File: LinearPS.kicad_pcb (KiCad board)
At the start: 2 copper layers, 100 x 100 mm, 91 parts, among them J1 Conn_01x03, J2 Conn_01x02, J3 Conn_01x03, J4 Conn_01x01, J5 Conn_01x01, J6 Conn_01x01, J7 Conn_01x01, J8 Conn_01x02, Q1 2N3904, Q2 TIP41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

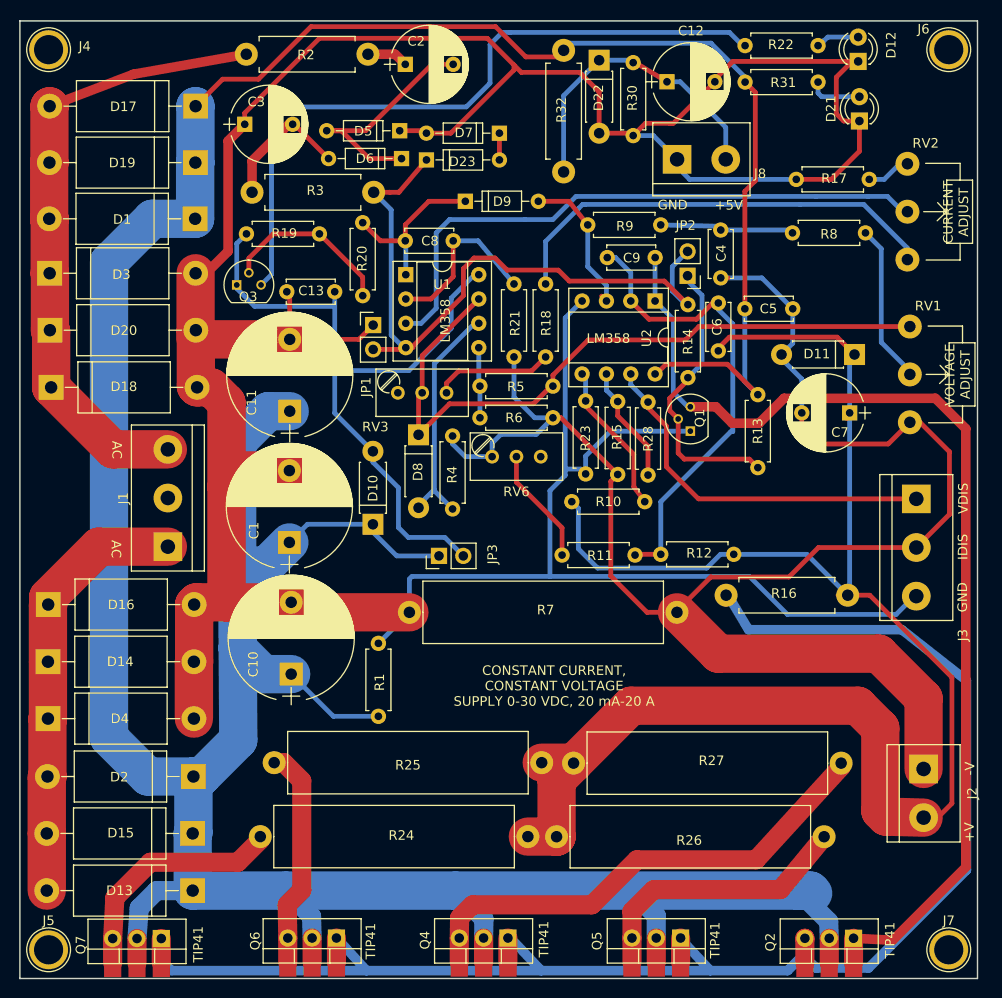
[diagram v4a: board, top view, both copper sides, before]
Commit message: Added external control input for current and voltage
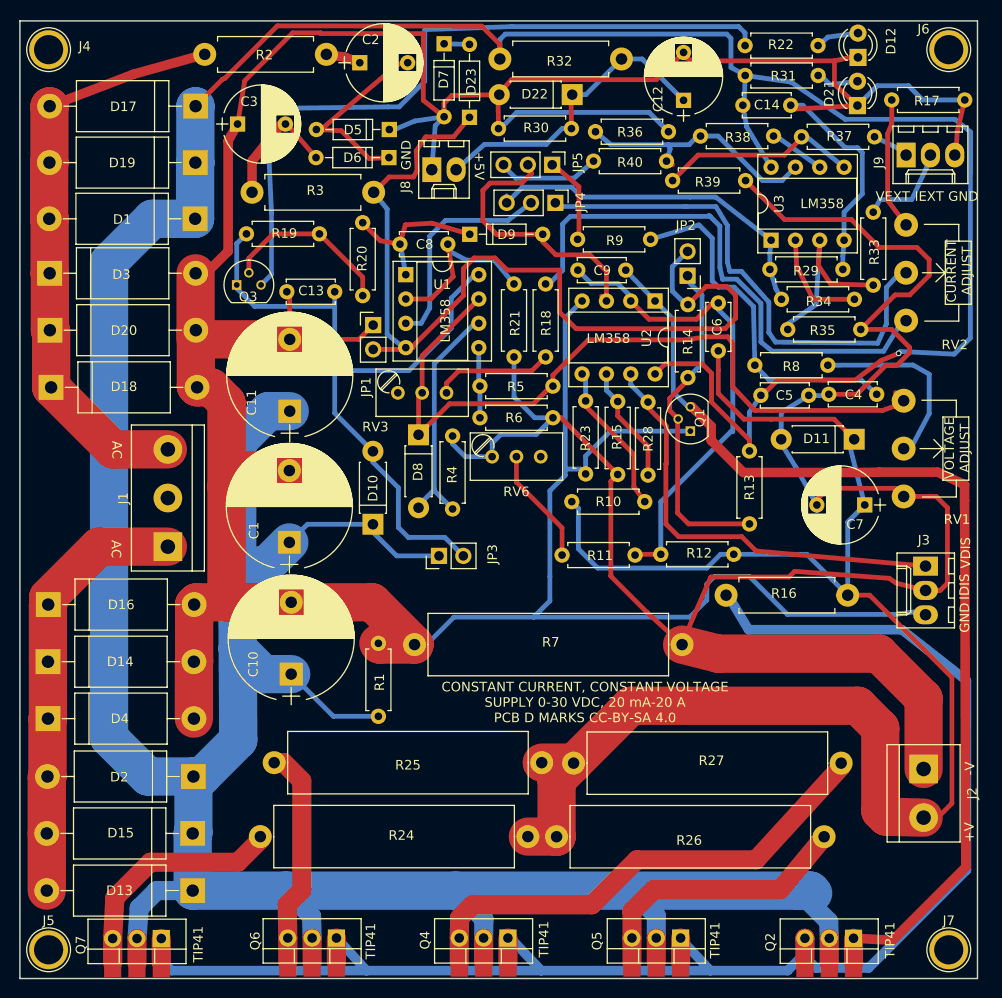
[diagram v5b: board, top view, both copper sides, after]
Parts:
- added C14: 100 nF, Capacitors_THT:C_Disc_D5.0mm_W2.5mm_P5.00mm, F.Cu at (130.5, 58.8)
- added J9: Conn_01x03, Connectors_Molex:Molex_KK-6410-03_03x2.54mm_Straight, F.Cu at (142.5, 64.0)
- added JP4: Jumper_NC_Dual, Pin_Headers:Pin_Header_Straight_1x03_Pitch2.54mm, F.Cu at (105.9, 69.0)
- added JP5: Jumper_NC_Dual, Pin_Headers:Pin_Header_Straight_1x03_Pitch2.54mm, F.Cu at (105.6, 65.0)
- added R29: 10k, Resistors_THT:R_Axial_DIN0207_L6.3mm_D2.5mm_P7.62mm_Horizontal, F.Cu at (128.3, 75.9)
- added R33: 10k, Resistors_THT:R_Axial_DIN0207_L6.3mm_D2.5mm_P7.62mm_Horizontal, F.Cu at (139.1, 77.6)
- added R34: 10k, Resistors_THT:R_Axial_DIN0207_L6.3mm_D2.5mm_P7.62mm_Horizontal, F.Cu at (129.5, 79.1)
- added R35: 10k, Resistors_THT:R_Axial_DIN0207_L6.3mm_D2.5mm_P7.62mm_Horizontal, F.Cu at (130.2, 82.2)
- added R36: 10k, Resistors_THT:R_Axial_DIN0207_L6.3mm_D2.5mm_P7.62mm_Horizontal, F.Cu at (117.7, 61.6)
- added R37: 10k, Resistors_THT:R_Axial_DIN0207_L6.3mm_D2.5mm_P7.62mm_Horizontal, F.Cu at (131.6, 62.1)
- added R38: 10k, Resistors_THT:R_Axial_DIN0207_L6.3mm_D2.5mm_P7.62mm_Horizontal, F.Cu at (128.7, 62.0)
- added R39: 10k, Resistors_THT:R_Axial_DIN0207_L6.3mm_D2.5mm_P7.62mm_Horizontal, F.Cu at (118.2, 66.7)
- added R40: 47k, Resistors_THT:R_Axial_DIN0207_L6.3mm_D2.5mm_P7.62mm_Horizontal, F.Cu at (109.9, 64.6)
- added U3: LM358, Housings_DIP:DIP-8_W7.62mm_Socket, F.Cu at (128.4, 72.9)
- J3: footprint Connectors_Terminal_Blocks:TerminalBlock_bornier-3_P5.08mm -> Connectors_Molex:Molex_KK-6410-03_03x2.54mm_Straight
- J8: footprint Connectors_Terminal_Blocks:TerminalBlock_bornier-2_P5.08mm -> Connectors_Molex:Molex_KK-6410-02_02x2.54mm_Straight
- moved J8 25.6 mm to (93.0, 65.5)
- moved C4 16.6 mm to (134.5, 89.0), turned to 0 degrees
- moved R8 14.4 mm to (126.8, 86.0)
- moved R32 13.3 mm to (112.8, 54.0), turned to 180 degrees
- moved D7 11.0 mm to (94.3, 52.4), turned to 270 degrees
- moved C7 9.74 mm to (138.2, 100.5)
- moved R30 9.43 mm to (107.6, 61.2), turned to 180 degrees
- moved C5 9.19 mm to (132.4, 89.1)
- moved D11 8.85 mm to (137.1, 93.7)
- moved R17 8.62 mm to (141.0, 58.3), turned to 0 degrees
- moved RV1 7.77 mm to (142.3, 89.7)
- moved J3 7.09 mm to (144.6, 106.9)
- moved RV2 6.38 mm to (142.5, 71.3)
- moved D23 6.32 mm to (97.0, 60.1), turned to 90 degrees
- moved R13 5.95 mm to (126.2, 102.5)
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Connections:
- R9 pad 1: Net-(D9-Pad2) -> Net-(JP5-Pad1)
- RV2 pad 2: Net-(RV2-Pad2) -> Net-(JP4-Pad1)
- U1 pad 3: Net-(RV2-Pad2) -> Net-(JP4-Pad2)
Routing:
- net Net-(RV2-Pad2): track 63.1 -> 0.00 mm
- net Net-(C1-Pad1): track 404.6 -> 467.5 mm, vias 0 -> 1
- net Net-(JP4-Pad1): track 0.00 -> 54.0 mm
- net GND: track 370.7 -> 416.5 mm
- net Net-(C4-Pad1): track 173.3 -> 218.6 mm
- net Net-(JP4-Pad3): track 0.00 -> 37.4 mm
- net Net-(R36-Pad2): track 0.00 -> 26.5 mm
- net Net-(D23-Pad1): track 75.0 -> 100.5 mm
- net Net-(JP4-Pad2): track 0.00 -> 23.0 mm
- net Net-(C4-Pad2): track 14.5 -> 37.2 mm
- net Net-(R37-Pad1): track 0.00 -> 21.0 mm
- net Net-(R33-Pad1): track 0.00 -> 20.3 mm
- net Net-(D9-Pad2): track 16.8 -> 30.8 mm
- net Net-(R34-Pad2): track 0.00 -> 10.9 mm
- net Net-(JP5-Pad3): track 0.00 -> 10.7 mm
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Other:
- board text added: "CONSTANT CURRENT, CONSTANT VOLTAGE SUPPLY 0-30 VDC, 20 mA-20 A PCB D MARKS CC-BY-SA 4.0"
- board text added: "IEXT"
- board text added: "VEXT"
- board text removed: "CONSTANT CURRENT, CONSTANT VOLTAGE SUPPLY 0-30 VDC, 20 mA-20 A"

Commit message: Fixed stupid mistake in external input
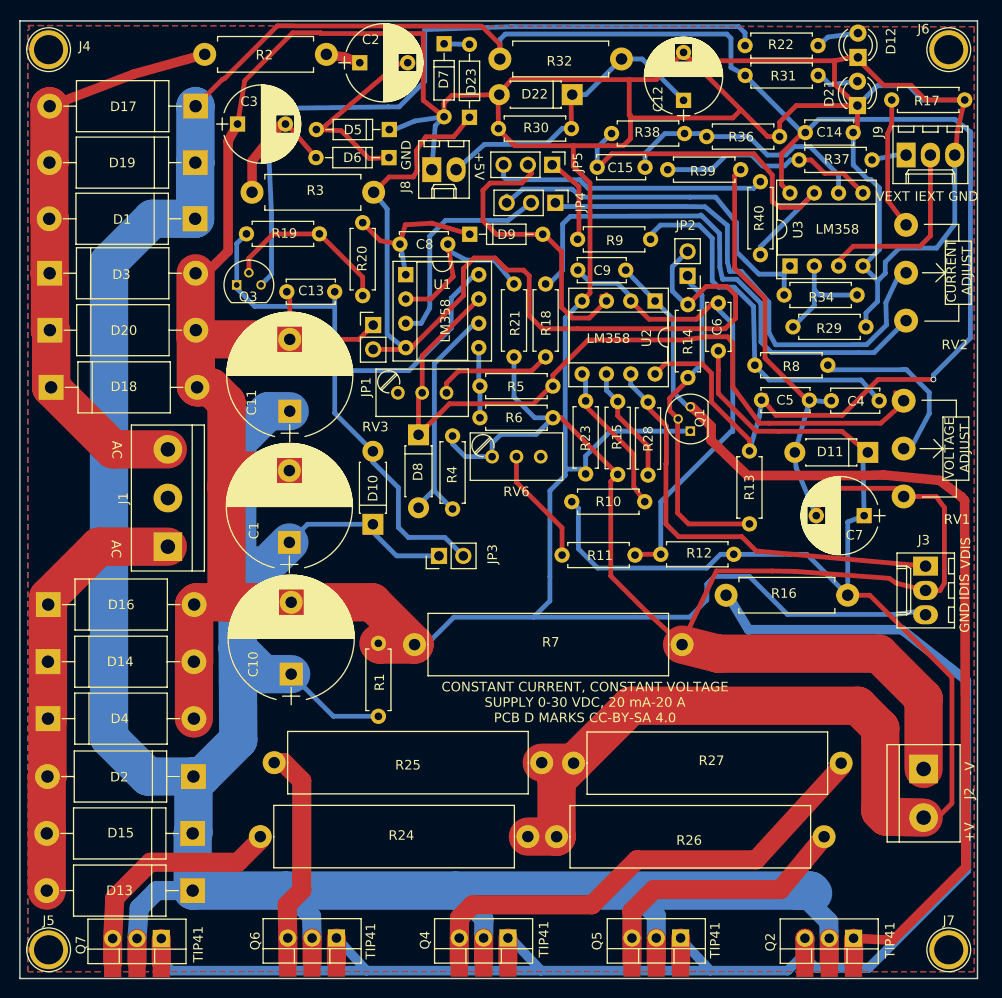
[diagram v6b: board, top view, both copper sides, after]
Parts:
- removed R33, R35: 10k, Resistors_THT:R_Axial_DIN0207_L6.3mm_D2.5mm_P7.62mm_Horizontal
- added C15: 100 pF, Capacitors_THT:C_Disc_D5.0mm_W2.5mm_P5.00mm, F.Cu at (110.3, 65.3)
- moved R40 17.6 mm to (127.3, 66.8), turned to 270 degrees
- moved R38 16.9 mm to (111.8, 61.8), turned to 0 degrees
- moved R36 11.6 mm to (129.3, 62.1)
- moved C14 7.12 mm to (137.0, 61.7)
- moved R29 6.47 mm to (130.7, 82.0)
- moved U3 3.34 mm to (130.4, 75.6)
- moved R37 2.43 mm to (131.4, 64.5)
- moved D11 1.98 mm to (138.5, 95.1)
- moved R39 1.25 mm to (117.7, 65.5)
- moved C7 1.12 mm to (138.2, 101.7)
- moved C4 0.72 mm to (134.7, 89.7)
- moved R34 0.53 mm to (129.8, 78.6)
- moved C5 0.50 mm to (132.4, 89.6)
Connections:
- J5 pad 1: (no net) -> GND
- J6 pad 1: (no net) -> GND
- R29 pad 1: Net-(JP4-Pad3) -> Net-(R29-Pad1)
- R34 pad 2: Net-(R34-Pad2) -> Net-(R29-Pad1)
- R36 pad 2: Net-(R36-Pad2) -> Net-(C15-Pad2)
- R38 pad 1: Net-(R38-Pad1) -> Net-(C15-Pad1)
- R38 pad 2: Net-(R36-Pad2) -> Net-(C15-Pad2)
- R40 pad 2: Net-(R36-Pad2) -> Net-(C15-Pad1)
- U3 pad 2: Net-(R34-Pad2) -> Net-(R29-Pad1)
- U3 pad 3: Net-(R33-Pad1) -> Net-(J9-Pad2)
- U3 pad 6: Net-(R38-Pad1) -> Net-(C15-Pad2)
- U3 pad 7: Net-(R36-Pad2) -> Net-(C15-Pad1)
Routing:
- net GND: track 416.5 -> 500.9 mm
- net Net-(C15-Pad1): track 0.00 -> 41.0 mm
- net Net-(C15-Pad2): track 0.00 -> 27.0 mm
- net Net-(R36-Pad2): track 26.5 -> 0.00 mm
- net Net-(C4-Pad1): track 218.6 -> 194.6 mm
- net Net-(R33-Pad1): track 20.3 -> 0.00 mm
- net Net-(JP5-Pad3): track 10.7 -> 29.3 mm
- net Net-(R29-Pad1): track 0.00 -> 12.0 mm
- net Net-(R34-Pad2): track 10.9 -> 0.00 mm
- net Net-(J9-Pad2): track 9.64 -> 20.0 mm
- net Net-(R38-Pad1): track 5.87 -> 0.00 mm
- net Net-(R37-Pad1): track 21.0 -> 24.7 mm
- net Net-(D9-Pad2): track 30.8 -> 33.4 mm
- net Net-(JP4-Pad3): track 37.4 -> 39.5 mm
- net Net-(D8-Pad1): track 80.5 -> 82.0 mm
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- added copper zone on B.Cu, net GND
- added copper zone on F.Cu, net GND

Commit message: Cleaned up schematic to make it easier to read
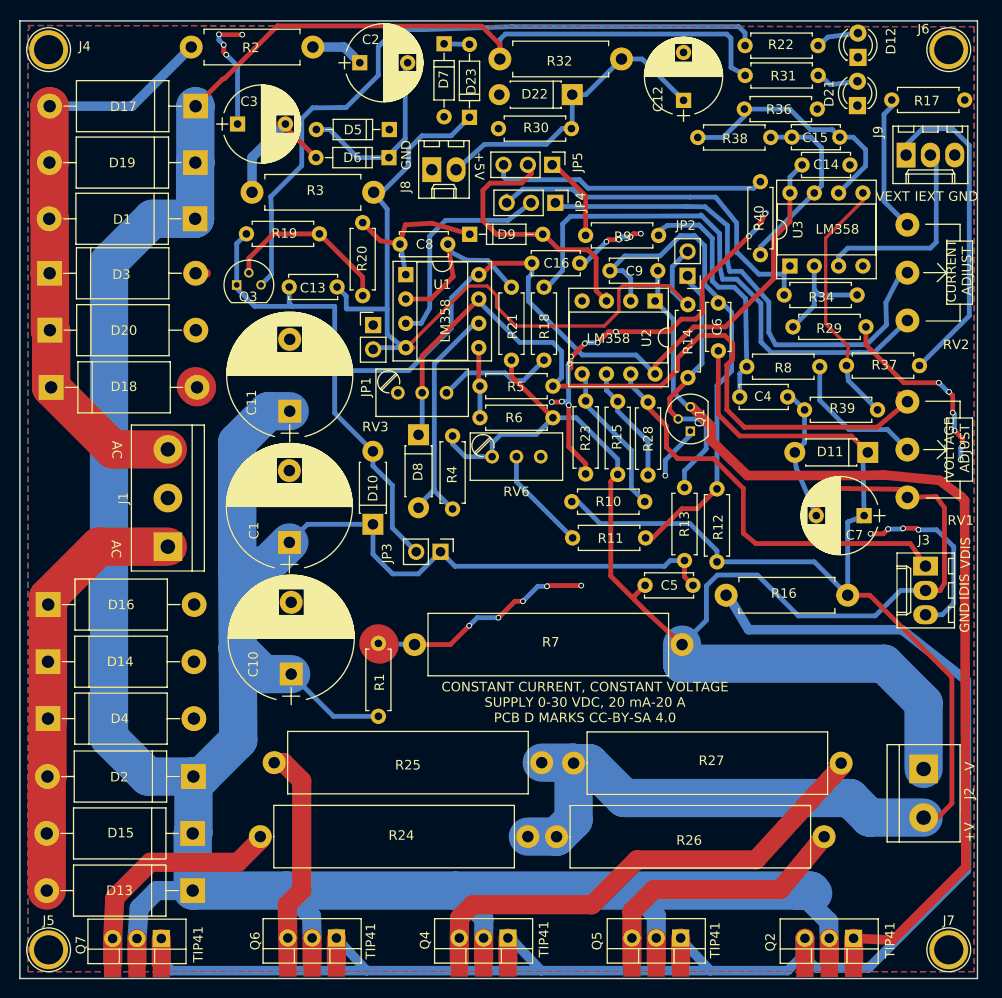
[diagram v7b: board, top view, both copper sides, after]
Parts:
- added C16: 100 nF, Capacitors_THT:C_Disc_D5.0mm_W2.5mm_P5.00mm, F.Cu at (108.5, 75.3)
- moved R39 33.3 mm to (139.6, 90.6), turned to 180 degrees
- moved C5 25.9 mm to (115.3, 108.9), turned to 0 degrees
- moved R37 22.0 mm to (136.3, 86.0)
- moved C15 20.6 mm to (130.6, 62.1)
- moved R38 16.6 mm to (128.4, 62.2), turned to 180 degrees
- moved R13 7.77 mm to (119.4, 98.7), turned to 270 degrees
- moved C13 5.27 mm to (83.1, 77.8), turned to 180 degrees
- moved R36 4.87 mm to (133.3, 59.2)
- moved C4 4.58 mm to (130.2, 89.3), turned to 180 degrees
- moved C14 3.40 mm to (136.7, 65.0)
- moved C9 3.35 mm to (116.6, 76.1)
- moved R11 2.10 mm to (107.7, 104.0)
- moved R12 1.92 mm to (122.8, 106.5), turned to 90 degrees
- moved R2 1.60 mm to (67.9, 52.7)
- moved R9 0.93 mm to (109.1, 72.4)
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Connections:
- C13 pad 1: GND -> Net-(C13-Pad1)
- C14 pad 2: Net-(C1-Pad1) -> Net-(C13-Pad2)
- D23 pad 1: Net-(D23-Pad1) -> Net-(C13-Pad1)
- JP1 pad 2: Net-(D23-Pad1) -> Net-(C13-Pad1)
- JP2 pad 2: Net-(D23-Pad1) -> Net-(C13-Pad1)
- R14 pad 1: Net-(D23-Pad1) -> Net-(C13-Pad1)
- R3 pad 1: Net-(D23-Pad1) -> Net-(C13-Pad1)
- U1 pad 4: Net-(D23-Pad1) -> Net-(C13-Pad1)
- U2 pad 8: Net-(C1-Pad1) -> Net-(C13-Pad2)
- U3 pad 8: Net-(C1-Pad1) -> Net-(C13-Pad2)
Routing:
- net GND: track 500.9 -> 142.7 mm, vias 0 -> 35
- net Net-(D23-Pad1): track 100.4 -> 0.00 mm
- net Net-(C13-Pad1): track 0.00 -> 91.5 mm
- net Net-(C1-Pad1): track 467.9 -> 395.3 mm, vias 1 -> 0
- net Net-(C13-Pad2): track 74.4 -> 127.3 mm
- net Net-(J9-Pad1): track 4.26 -> 34.7 mm
- net Net-(C4-Pad1): track 194.6 -> 172.2 mm
- net Net-(C15-Pad1): track 41.0 -> 19.9 mm
- net Net-(C4-Pad2): track 38.6 -> 26.6 mm
- net Net-(C6-Pad1): track 173.5 -> 162.0 mm
- net Net-(JP2-Pad1): track 35.2 -> 28.4 mm
- net Net-(C6-Pad2): track 50.6 -> 55.6 mm
- net Net-(Q3-Pad3): track 77.4 -> 73.2 mm
- net Net-(R8-Pad2): track 19.7 -> 16.6 mm
- net Net-(D9-Pad2): track 33.4 -> 30.7 mm
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
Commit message: Modified for larger diode and capactior footprints, TO-220 and TO-247 devices
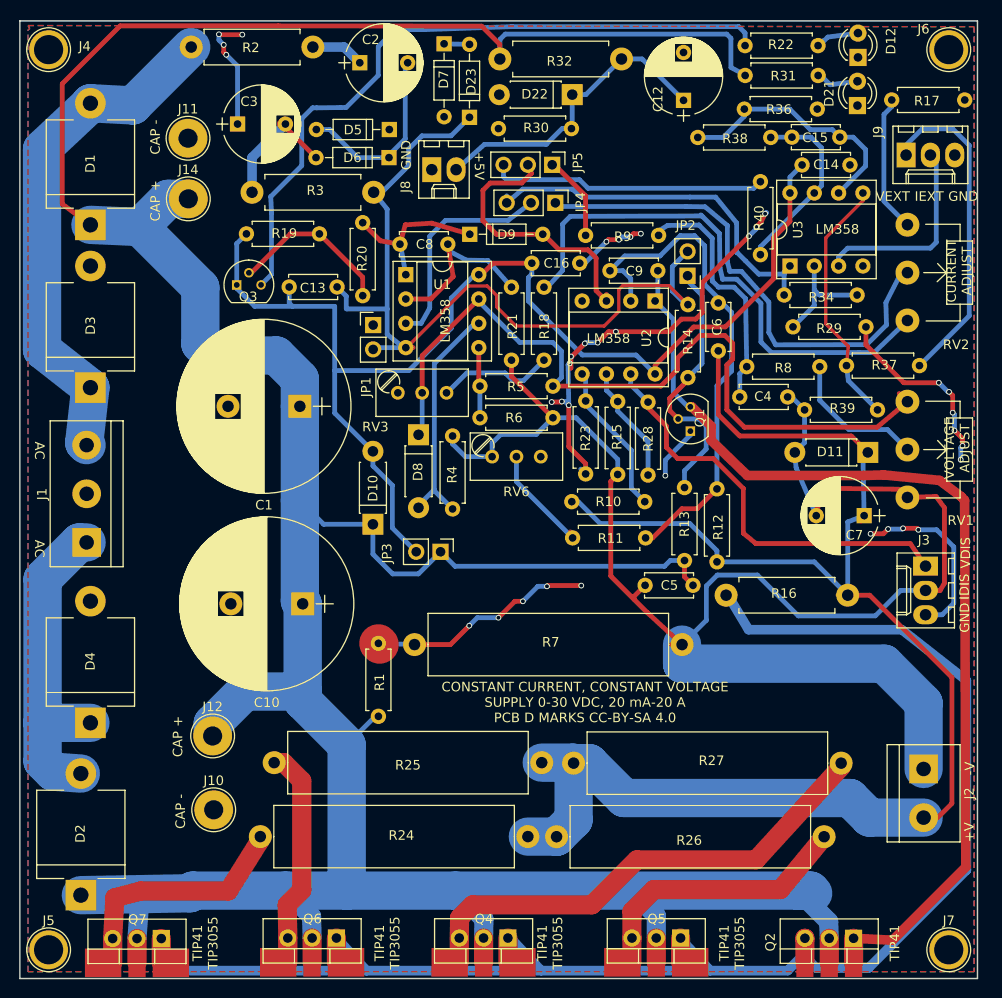
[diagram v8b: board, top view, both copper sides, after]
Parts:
- removed C11: CP, Capacitors_THT:CP_Radial_D13.0mm_P7.50mm
- removed D13, D14, D15, D16, D17, D18, D19, D20: 10A10, Diodes_THT:D_DO-201_P15.24mm_Horizontal
- added J10: Conn_01x01, Connectors:1pin, F.Cu at (70.2, 132.4)
- added J11: Conn_01x01, Connectors:1pin, F.Cu at (67.6, 62.3)
- added J12: Conn_01x01, Connectors:1pin, F.Cu at (70.1, 124.7)
- added J14: Conn_01x01, Connectors:1pin, F.Cu at (67.6, 68.6)
- C1, C10: footprint Capacitors_THT:CP_Radial_D13.0mm_P7.50mm -> Capacitors_THT:CP_Radial_D18.0mm_P7.50mm
- D1, D2, D3, D4: footprint Diodes_THT:D_DO-201_P15.24mm_Horizontal -> Diodes_THT:D_P600_R-6_P12.70mm_Horizontal
- Q4, Q5, Q6, Q7: footprint linearps:TO-220-3_Vertical_WithPads -> linearps:TO-220-3_Vertical_WithBigPads
- moved D2 17.1 mm to (56.4, 141.3), turned to 90 degrees
- moved C1 14.3 mm to (79.2, 90.2), turned to 180 degrees
- moved D3 12.7 mm to (57.4, 88.3), turned to 90 degrees
- moved D1 11.0 mm to (57.4, 71.3), turned to 90 degrees
- moved J1 8.50 mm to (57.0, 104.5)
- moved C10 7.44 mm to (79.5, 110.9), turned to 180 degrees
- moved D4 4.45 mm to (57.4, 123.3), turned to 90 degrees
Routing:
- net Net-(C1-Pad1): track 395.3 -> 382.7 mm
- net Net-(D2-Pad2): track 45.4 -> 34.7 mm
- net Net-(D1-Pad2): track 61.7 -> 53.5 mm
- net GND: track 142.7 -> 141.2 mm
- net Net-(Q3-Pad2): track 18.3 -> 17.4 mm
- net Net-(Q7-Pad3): track 24.8 -> 25.4 mm
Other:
- board text added: "CAP +"
- board text added: "CAP -"
- board text added: "TIP41 TIP3055"
